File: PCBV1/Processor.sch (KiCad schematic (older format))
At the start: 2 parts

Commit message: Made a bunch of very small changes.
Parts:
- added C? (x3): 22µ, symbol Device:C
- added C? (x2): 4.7µ, symbol Device:C
- added C? (x13): 220n, symbol Device:C
- added C?: 10µ, symbol Device:C
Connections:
- net GND: now also C?.2, C?.2, C?.2, C?.2, C?.2, C?.2, C?.2, C?.2, C?.2, C?.2, C?.2, C?.2, C?.2, C?.2, C?.2, C?.2, C?.2, C?.2, C?.2
- net at U?.G10 (VDD_ARM_CAP_2): now also U?.G11 (VDD_ARM_CAP_3), U?.G9 (VDD_ARM_CAP_1), C?.1, C?.1, C?.1
- net DRAM_A6: now reaches U?.G2 (DRAM_ADDR06)
- net DRAM_RESET: now reaches U?.G4 (DRAM_RESET)
- net at U?.G8 (VDD_SOC_CAP_1): now also C?.1
- net +1V35: now reaches U?.H10 (VDD_SOC_IN_2)
- net +1V35: now also U?.H9 (VDD_SOC_IN_1), U?.J10 (VDD_SOC_IN_4), U?.J9 (VDD_SOC_IN_3), U?.K10 (VDD_SOC_IN_6), U?.K9 (VDD_SOC_IN_5), C?.1, C?.1, C?.1, C?.1
- net DRAM_A1: now reaches U?.H2 (DRAM_ADDR01)
- net DRAM_A13: now reaches U?.H3 (DRAM_ADDR13)
- net DRAM_A7: now reaches U?.H4 (DRAM_ADDR07)
- net at U?.H8 (VDD_SOC_CAP_2): now also C?.1
- net DRAM_A8: now reaches U?.J4 (DRAM_ADDR08)
- net DRAM_A2: now reaches U?.K1 (DRAM_ADDR02)
- net DRAM_A11: now reaches U?.K3 (DRAM_ADDR11)
- net DRAM_A4: now reaches U?.K4 (DRAM_ADDR04)
- net DRAM_A5: now reaches U?.L1 (DRAM_ADDR05)
- net at U?.L10 (VDD_SOC_CAP_9): now also U?.L11 (VDD_SOC_CAP_10), U?.L8 (VDD_SOC_CAP_7), U?.L9 (VDD_SOC_CAP_8), C?.1, C?.1, C?.1, C?.1
- net DRAM_A9: now reaches U?.L2 (DRAM_ADDR09)
- net DRAM_A12: now reaches U?.L4 (DRAM_ADDR12)
- net DRAM_A0: now reaches U?.L5 (DRAM_ADDR00)
- net DRAM_A3: now reaches U?.M2 (DRAM_ADDR03)
- net DRAM_A10: now reaches U?.M4 (DRAM_ADDR10)
- net at U?.N12 (VDD_SNVS_CAP): now also C?.1
- net +3V3: now reaches U?.N13 (VDD_HIGH_IN)
- net +3V3: now also U?.P12 (VDD_SNVS_IN), U?.R14 (VDD_HIGH_CAP_1), U?.R15 (VDD_HIGH_CAP_2), C?.1, C?.1, C?.1, C?.1, C?.1
- net DRAM_D13: now reaches U?.P3 (DRAM_DATA13)
- net DRAM_VREF: now reaches U?.P4 (DRAM_VREF)
- net DRAM_D12: now reaches U?.P5 (DRAM_DATA12)
- net DRAM_D15: now reaches U?.R1 (DRAM_DATA15)
- net DRAM_D14: now reaches U?.R2 (DRAM_DATA14)
- net DRAM_D11: now reaches U?.R4 (DRAM_DATA11)
- net DRAM_D0: now reaches U?.T4 (DRAM_DATA00)
- net DRAM_D6: now reaches U?.T5 (DRAM_DATA06)
- net DRAM_D2: now reaches U?.T6 (DRAM_DATA02)
- net DRAM_D5: now reaches U?.T8 (DRAM_DATA05)
- net DRAM_D8: now reaches U?.U2 (DRAM_DATA08)
- net DRAM_D9: now reaches U?.U3 (DRAM_DATA09)
- net DRAM_D7: now reaches U?.U4 (DRAM_DATA07)
- net DRAM_D10: now reaches U?.U5 (DRAM_DATA10)
- net DRAM_D1: now reaches U?.U6 (DRAM_DATA01)
- net DRAM_D3: now reaches U?.U7 (DRAM_DATA03)
- net DRAM_D4: now reaches U?.U8 (DRAM_DATA04)
- no-connect marks 0 -> 2
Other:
- note added: "NÅET TIL NVCC_DRAM I HARDWARE DESIGN CHECKLISTEN"
- moved on the sheet: R?, U?

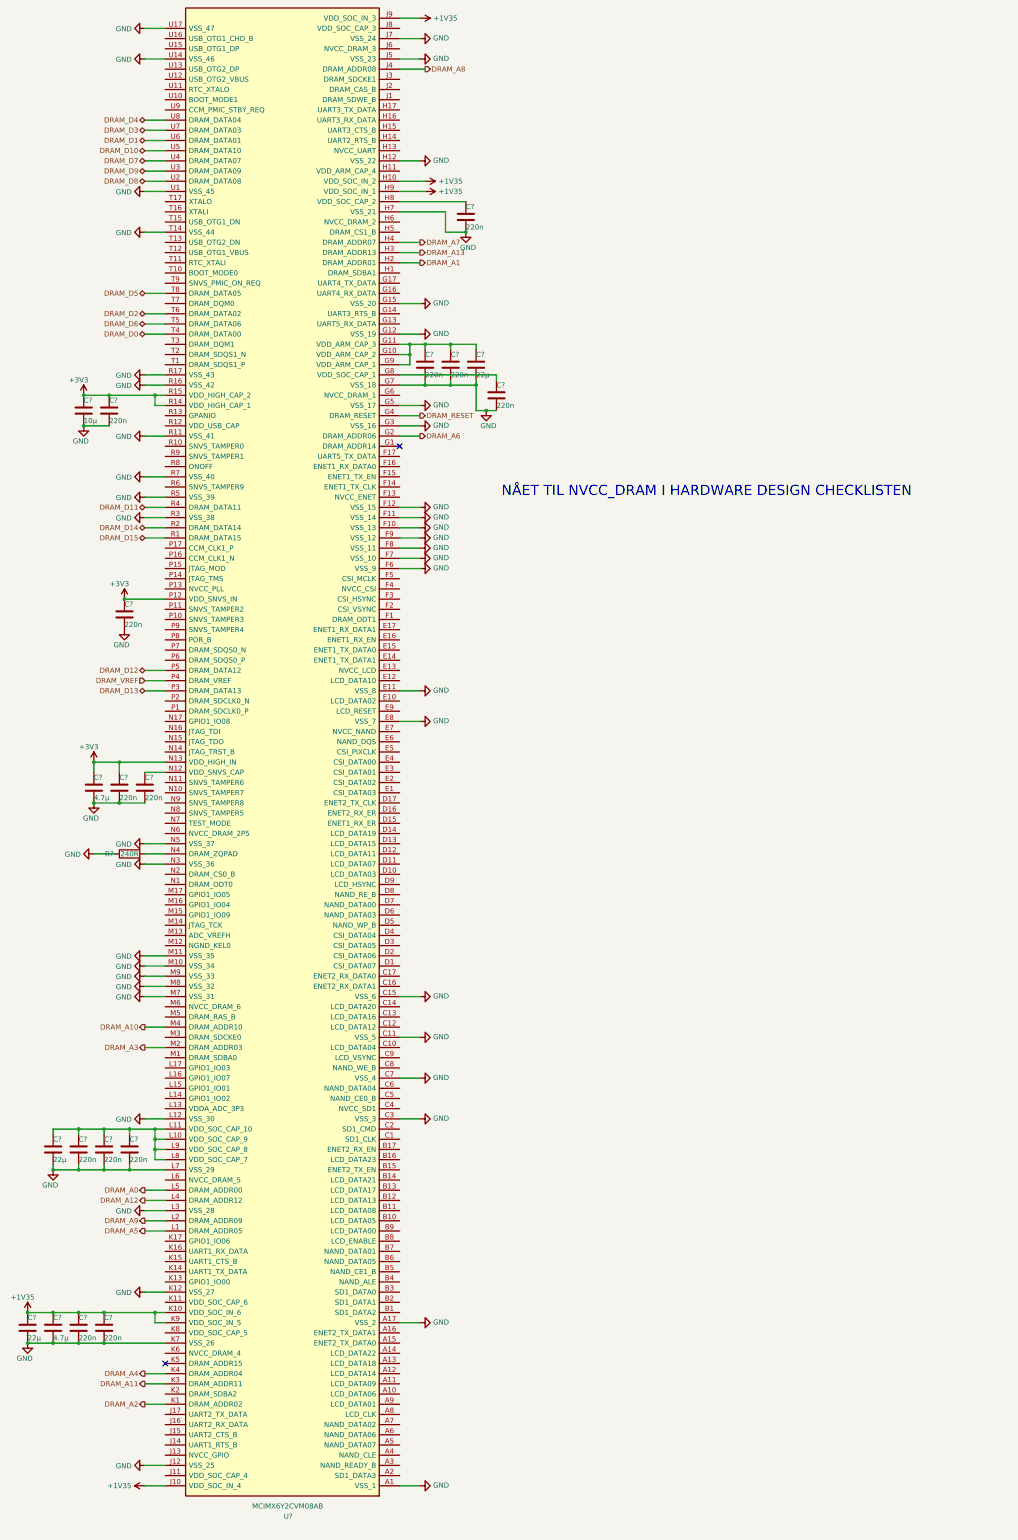
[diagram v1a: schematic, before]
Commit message: Added UART, modifications to video etc.
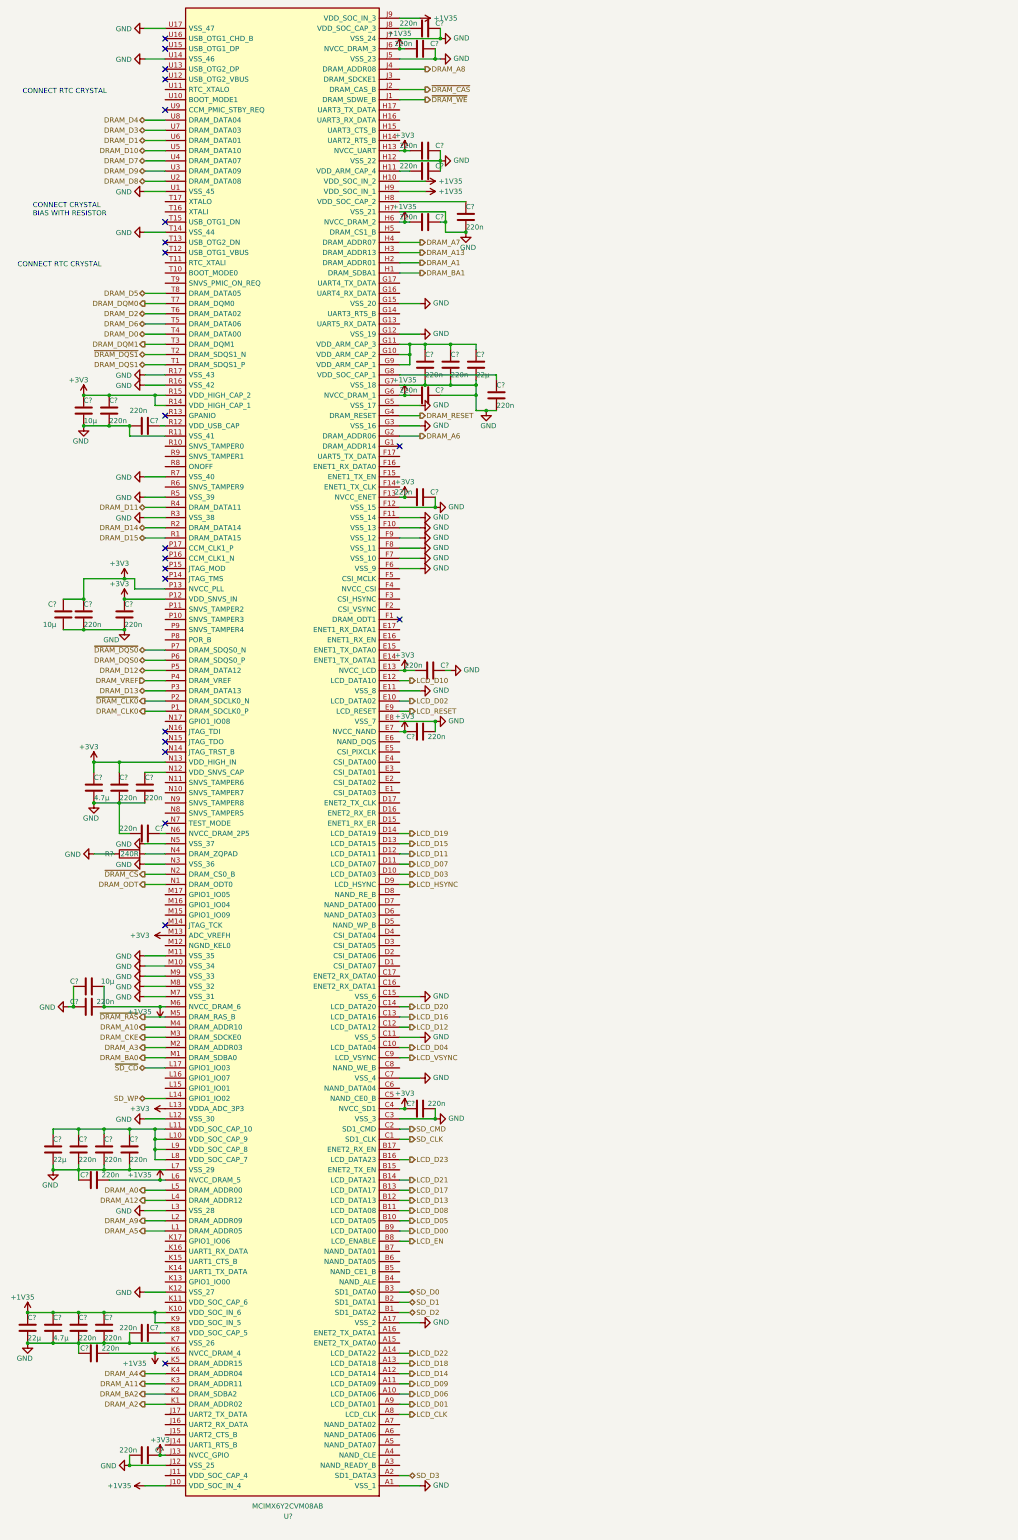
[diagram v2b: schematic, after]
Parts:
- added C? (x18): 220n, symbol Device:C
- added C? (x2): 10µ, symbol Device:C
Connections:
- net +1V35: now also U?.G6 (NVCC_DRAM_1), U?.H6 (NVCC_DRAM_2), U?.J6 (NVCC_DRAM_3), U?.K6 (NVCC_DRAM_4), U?.L6 (NVCC_DRAM_5), U?.M6 (NVCC_DRAM_6), C?.2, C?.2, C?.2, C?.2, C?.2, C?.2, C?.2
- net +3V3: now also U?.C4 (NVCC_SD1), U?.E13 (NVCC_LCD), U?.E7 (NVCC_NAND), U?.F13 (NVCC_ENET), U?.H13 (NVCC_UART), U?.J13 (NVCC_GPIO), U?.L13 (VDDA_ADC_3P3), U?.M13 (ADC_VREFH), U?.P13 (NVCC_PLL), C?.1, C?.1, C?.1, C?.1, C?.1, C?.2, C?.2, C?.2
- net GND: now also C?.1, C?.1, C?.1, C?.1, C?.1, C?.1, C?.1, C?.1, C?.1, C?.1, C?.1, C?.1, C?.2, C?.2, C?.2, C?.2, C?.2, C?.2, C?.2, C?.2
- net LCD_D06: now reaches U?.A10 (LCD_DATA06)
- net LCD_D09: now reaches U?.A11 (LCD_DATA09)
- net LCD_D14: now reaches U?.A12 (LCD_DATA14)
- net LCD_D18: now reaches U?.A13 (LCD_DATA18)
- net LCD_D22: now reaches U?.A14 (LCD_DATA22)
- net SD_D3: now reaches U?.A2 (SD1_DATA3)
- net LCD_CLK: now reaches U?.A8 (LCD_CLK)
- net LCD_D01: now reaches U?.A9 (LCD_DATA01)
- net SD_D2: now reaches U?.B1 (SD1_DATA2)
- net LCD_D05: now reaches U?.B10 (LCD_DATA05)
- net LCD_D08: now reaches U?.B11 (LCD_DATA08)
- net LCD_D13: now reaches U?.B12 (LCD_DATA13)
- net LCD_D17: now reaches U?.B13 (LCD_DATA17)
- net LCD_D21: now reaches U?.B14 (LCD_DATA21)
- net LCD_D23: now reaches U?.B16 (LCD_DATA23)
- net SD_D1: now reaches U?.B2 (SD1_DATA1)
- net SD_D0: now reaches U?.B3 (SD1_DATA0)
- net LCD_EN: now reaches U?.B8 (LCD_ENABLE)
- net LCD_D00: now reaches U?.B9 (LCD_DATA00)
- net SD_CLK: now reaches U?.C1 (SD1_CLK)
- net LCD_D04: now reaches U?.C10 (LCD_DATA04)
- net LCD_D12: now reaches U?.C12 (LCD_DATA12)
- net LCD_D16: now reaches U?.C13 (LCD_DATA16)
- net LCD_D20: now reaches U?.C14 (LCD_DATA20)
- net SD_CMD: now reaches U?.C2 (SD1_CMD)
- net LCD_VSYNC: now reaches U?.C9 (LCD_VSYNC)
- net LCD_D03: now reaches U?.D10 (LCD_DATA03)
- net LCD_D07: now reaches U?.D11 (LCD_DATA07)
- net LCD_D11: now reaches U?.D12 (LCD_DATA11)
- net LCD_D15: now reaches U?.D13 (LCD_DATA15)
- net LCD_D19: now reaches U?.D14 (LCD_DATA19)
- net LCD_HSYNC: now reaches U?.D9 (LCD_HSYNC)
- net LCD_D02: now reaches U?.E10 (LCD_DATA02)
- net LCD_D10: now reaches U?.E12 (LCD_DATA10)
- net LCD_RESET: now reaches U?.E9 (LCD_RESET)
- net DRAM_BA1: now reaches U?.H1 (DRAM_SDBA1)
- net at U?.H11 (VDD_ARM_CAP_4): now also C?.2
- net ~DRAM_WE: now reaches U?.J1 (DRAM_SDWE_B)
- net ~DRAM_CAS: now reaches U?.J2 (DRAM_CAS_B)
- net at U?.J8 (VDD_SOC_CAP_3): now also C?.2
- net DRAM_BA2: now reaches U?.K2 (DRAM_SDBA2)
- net at U?.K8 (VDD_SOC_CAP_5): now also C?.1
- net SD_WP: now reaches U?.L14 (GPIO1_IO02)
- net ~SD_CD: now reaches U?.L17 (GPIO1_IO03)
- net DRAM_BA0: now reaches U?.M1 (DRAM_SDBA0)
- net DRAM_CKE: now reaches U?.M3 (DRAM_SDCKE0)
- net ~DRAM_RAS: now reaches U?.M5 (DRAM_RAS_B)
- net DRAM_ODT: now reaches U?.N1 (DRAM_ODT0)
- net ~DRAM_CS: now reaches U?.N2 (DRAM_CS0_B)
- net at U?.N6 (NVCC_DRAM_2P5): now also C?.1
- net DRAM_CLK0: now reaches U?.P1 (DRAM_SDCLK0_P)
- net ~DRAM_CLK0: now reaches U?.P2 (DRAM_SDCLK0_N)
- net DRAM_DQS0: now reaches U?.P6 (DRAM_SDQS0_P)
- net ~DRAM_DQS0: now reaches U?.P7 (DRAM_SDQS0_N)
- net at U?.R12 (VDD_USB_CAP): now also C?.1
- net DRAM_DQS1: now reaches U?.T1 (DRAM_SDQS1_P)
- net ~DRAM_DQS1: now reaches U?.T2 (DRAM_SDQS1_N)
- net DRAM_DQM1: now reaches U?.T3 (DRAM_DQM1)
- net DRAM_DQM0: now reaches U?.T7 (DRAM_DQM0)
- no-connect marks 2 -> 21
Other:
- note added: "CONNECT CRYSTAL\nBIAS WITH RESISTOR"
- note added: "CONNECT RTC CRYSTAL"
- note removed: "NÅET TIL NVCC_DRAM I HARDWARE DESIGN CHECKLISTEN"
